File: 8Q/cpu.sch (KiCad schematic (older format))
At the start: 1 part

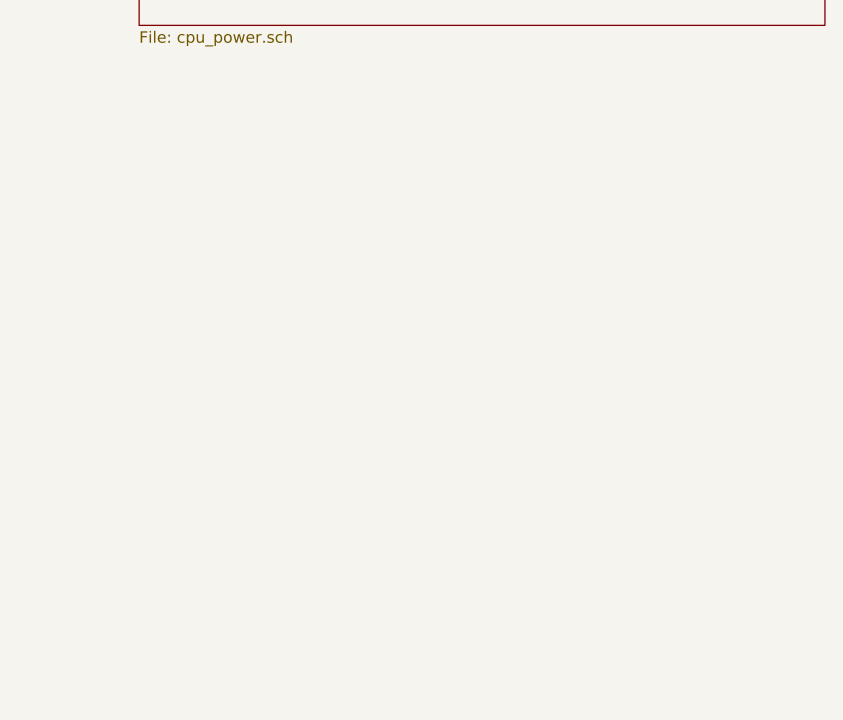
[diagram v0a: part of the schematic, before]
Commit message: modified:   8Q/8Q-cache.lib 	modified:   8Q/8Q.sch 	modified:   8Q/8_qp_io.sch 	new file:   8Q/RAM.sch 	deleted:    8Q/_saved_RAM.sch 	modified:   8Q/cpu.sch 	modified:   8Q/cpu_power.sch 	modified:   8Q/power.sch 	modified:   8Q/preprocessor.sch 	modified:   8Q/qpower.sch 	modified:   8Q/qpu.sch 	new file:   8q.dia 	modified:   README.md 	new file:   docs/source/imgs/8q.png
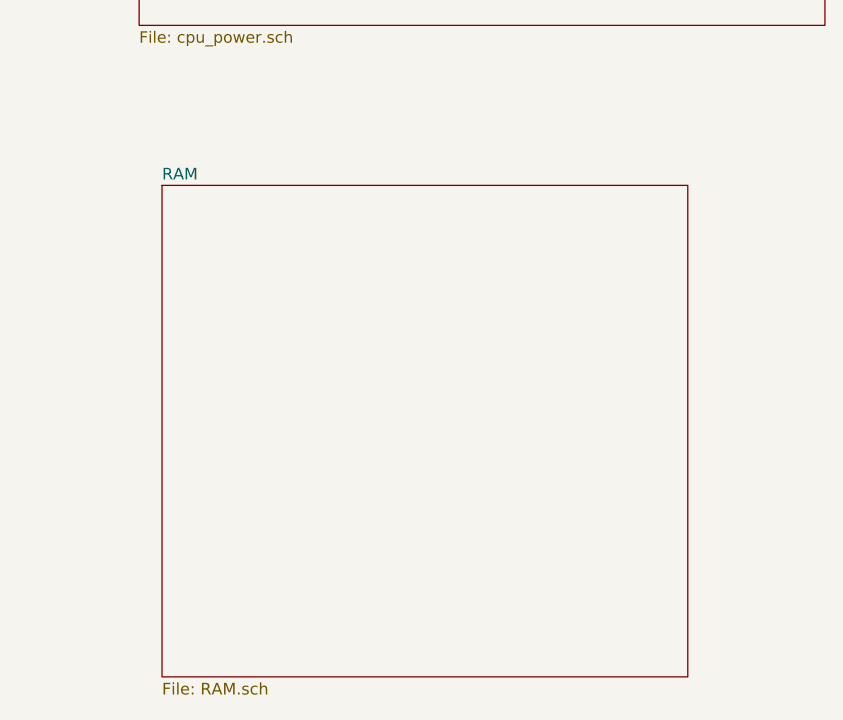
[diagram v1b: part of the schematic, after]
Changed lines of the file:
@@
 $Descr A4 11693 8268
 encoding utf-8
-Sheet 2 8
+Sheet 2 9
 Title "8Q Quantum Computer"
 Date "2020-06-29"
@@
 F1 "cpu_power.sch" 50
 $EndSheet
+$Sheet
+S 11850 3750 2300 2150
+U 5F329712
+F0 "RAM" 51
+F1 "RAM.sch" 51
+$EndSheet
 $EndSCHEMATC

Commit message: modified:   8Q/8Q-cache.lib 	modified:   8Q/8Q.sch 	modified:   8Q/8_qp_io.sch 	modified:   8Q/RAM.sch 	new file:   8Q/control_logic.sch 	modified:   8Q/cpu.sch 	modified:   8Q/cpu_power.sch 	new file:   8Q/inorder.sch 	new file:   8Q/instruction_bus.sch 	new file:   8Q/output_cache.sch 	modified:   8Q/power.sch 	modified:   8Q/preprocessor.sch 	modified:   8Q/qpower.sch 	modified:   8Q/qpu.sch 	new file:   Controller.md 	modified:   QCore.md 	new file:   QPU_Operation.md 	new file:   docs/source/imgs/Screenshot from 2020-07-07 18-04-51.png 	new file:   tools/photon_birth_death.py 	new file:   tools/processor.py
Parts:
- added J1: HDMI_A, Connector_HDMI:HDMI_A_Contact_Technology_HDMI-19APL2_Horizontal, symbol Connector:HDMI_A
- added unit 2 of U1
- added unit 3 of U1
- added unit 4 of U1
- added unit 5 of U1
- added U2: H5AN8G8NAFR-UHC, Package_BGA:FBGA-78_7.5x11mm_Layout2x3x13_P0.8mm, symbol Memory_RAM:H5AN8G8NAFR-UHC
- gave numbers to parts that had none: 1
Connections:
- net labels added: GND, HDMI_CEC, HDMI_SCL, HDMI_SDA, HDMI_UTIL, HDMI_VCC, HDMI_VDD, RAM_A0, RAM_A1, RAM_A10, RAM_A11, RAM_A12, RAM_A13, RAM_A14, RAM_A15, RAM_A16, RAM_A17, RAM_A2, RAM_A3, RAM_A4, RAM_A5, RAM_A6, RAM_A7, RAM_A8, RAM_A9, RAM_ACT, RAM_CKE0, RAM_CKE1, RAM_PARITY, RAM_RESET
- wire segments 0 -> 33
- no-connect marks 0 -> 2
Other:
- moved on the sheet: U1A

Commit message: modified:   8Q/8Q-cache.lib 	new file:   8Q/8Q-rescue.dcm 	new file:   8Q/8Q-rescue.lib 	modified:   8Q/8Q.kicad_pcb 	modified:   8Q/8Q.sch 	modified:   8Q/8_qp_io.sch 	new file:   8Q/QGates.pretty/CH-Gate.kicad_mod 	new file:   8Q/QGates.pretty/CX-Gate.kicad_mod 	new file:   8Q/QGates.pretty/CY-Gate.kicad_mod 	new file:   8Q/QGates.pretty/CZ-Gate.kicad_mod 	new file:   8Q/QGates.pretty/H-Gate.kicad_mod 	new file:   8Q/QGates.pretty/Measure.kicad_mod 	new file:   8Q/QGates.pretty/Photon-Source.kicad_mod 	new file:   8Q/QGates.pretty/X-Gate.kicad_mod 	new file:   8Q/QGates.pretty/Y-Gate.kicad_mod 	new file:   8Q/QGates.pretty/Z-Gate.kicad_mod 	modified:   8Q/control_logic.sch 	modified:   8Q/cpu.sch 	modified:   8Q/inorder.sch 	modified:   8Q/instruction_bus.sch 	modified:   8Q/output_cache.sch 	modified:   8Q/power.sch 	modified:   8Q/preprocessor.sch 	modified:   8Q/qpower.sch 	modified:   8Q/qpu.sch 	new file:   8Q/sym-lib-table Introduced embedded QSeven module to replace CPU Computer now has support for: * 10Gbps Ethernet * 1xUSB3.0 * 4xUSB2.0 * 1xJTAG * 1xCAN * 1-Wire Bus * 1xSMBus * 1xI2C * External Watchdog * HDMI * LVDS
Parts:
- removed J1: HDMI_A, Connector_HDMI:HDMI_A_Contact_Technology_HDMI-19APL2_Horizontal, symbol Connector:HDMI_A
- removed U1: ALLWINNER_H6_V200, BGA451C65P23X23_1500X1500X118N, symbol ALLWINNER_H6_V200:ALLWINNER_H6_V200
- removed U2: H5AN8G8NAFR-UHC, Package_BGA:FBGA-78_7.5x11mm_Layout2x3x13_P0.8mm, symbol Memory_RAM:H5AN8G8NAFR-UHC
- added BT1: Battery_Cell, symbol Device:Battery_Cell
- added C262292_1, C262292_2: LVDS Display, Connector_FFC-FPC:Hirose_FH12-40S-0.5SH_1x40-1MP_P0.50mm_Horizontal, symbol Connector:Conn_01x40_Female
- added D1: GreenLED, LED_SMD:LED_0603_1608Metric, symbol Device:LED
- added D10, D11, D12, D13, D14, D15, D16, D17, D18, D19, D20, D5, D6, D7, D8, D9: 1SS367,H3F, Diode_SMD:D_SOD-323, symbol Device:D_Schottky
- added D2: BlueLED, LED_SMD:LED_0603_1608Metric, symbol Device:LED
- added D3, D4: D_Small, symbol Device:D_Small
- added FL1, FL2, FL3, FL4, FL5: EMI_Filter_CommonMode, symbol Device:EMI_Filter_CommonMode
- added J1: TEMP, Connector_PinHeader_1.00mm:PinHeader_1x02_P1.00mm_Vertical, symbol Connector:Conn_01x02_Female
- added J10, J11, J16, J17: Bus_PCI_Express_x1, Connector_PCBEdge:BUS_PCIexpress_x1, symbol Connector2:Bus_PCI_Express_x1
- added J12: 8P8C_LED_Shielded, Connector_RJ:RJ45_Amphenol_54602-x08_Horizontal, symbol Connector:8P8C_LED_Shielded
- added J13: Watchdog, Connector_PinHeader_1.00mm:PinHeader_1x02_P1.00mm_Vertical, symbol Connector:Conn_01x02_Female
- added J14: Bus_PCI_Express_x4, Connector_PCBEdge:BUS_PCIexpress_x4, symbol Connector2:Bus_PCI_Express_x4
- added J15: SD_Card, Connector_Card:microSD_HC_Hirose_DM3AT-SF-PEJM5, symbol Connector2:SD_Card
- added J18: HDMI_A, symbol Connector:HDMI_A
- added J19: BIOS_DISABLE, Connector_PinHeader_1.00mm:PinHeader_1x02_P1.00mm_Vertical, symbol Connector:Conn_01x02_Female
- added J2: 1 WIRE BUS, Connector_PinHeader_1.00mm:PinHeader_1x01_P1.00mm_Vertical, symbol Connector:Conn_01x01_Female
- added J20: AVR-JTAG-10, Connector_IDC:IDC-Header_2x04_P2.54mm_Vertical, symbol Connector:AVR-JTAG-10
- added J21: USB3_A, Connector_USB:USB3_A_Molex_48393-001, symbol Connector:USB3_A
- added J22: LDC, Connector_IDC:IDC-Header_2x04_P2.54mm_Vertical, symbol Connector_Generic:Conn_02x04_Counter_Clockwise
- added J23: GPIO, Connector_PinHeader_1.00mm:PinHeader_1x08_P1.00mm_Vertical, symbol Connector:Conn_01x08_Female
- added J24, J25, J26, J27, J28: USB_A, Connector_USB:USB3_A_Molex_48393-001, symbol Connector2:USB_A
- added J3: SMBUS, Connector_PinHeader_1.00mm:PinHeader_1x03_P1.00mm_Vertical, symbol Connector:Conn_01x03_Female
- added J4: GP0_I2C, Connector_PinHeader_1.00mm:PinHeader_1x02_P1.00mm_Vertical, symbol Connector:Conn_01x02_Female
- added J5: HDA/I2C, Connector_PinHeader_1.00mm:PinHeader_1x05_P1.00mm_Vertical, symbol Connector:Conn_01x05_Female
- added J6: SATA0, Connector_SATA_SAS:SATA_Amphenol_10029364-001LF_Horizontal, symbol Connector:Conn_01x07_Female
- added J7: SATA1, Connector_SATA_SAS:SATA_Amphenol_10029364-001LF_Horizontal, symbol Connector:Conn_01x07_Female
- added J8: CAN BUS, Connector_PinHeader_1.00mm:PinHeader_1x02_P1.00mm_Vertical, symbol Connector:Conn_01x02_Female
- added J9: UART, Connector_PinHeader_1.00mm:PinHeader_1x04_P1.00mm_Vertical, symbol Connector:Conn_01x04_Male
- added M9: CPU_FAN, Connector:FanPinHeader_1x04_P2.54mm_Vertical, symbol Motor:Fan_4pin
- added Q1, Q2, Q3, Q4: Q_PNP_BCE, Package_TO_SOT_SMD:SOT-23, symbol Device:Q_PNP_BCE
- added Q5: Q_NPN_BCE, Package_TO_SOT_SMD:SOT-23, symbol Device:Q_NPN_BCE
- added Q6: Q7, Connector:MXM2.0, symbol Q7:Q7
- added R1, R2, R3, R4: 10k, Resistor_SMD:R_0402_1005Metric, symbol Device:R_Small_US
- added R10: 1M, Resistor_SMD:R_0402_1005Metric, symbol Device:R_Small_US
- added R5, R6, R7, R8: 1k, Resistor_SMD:R_0402_1005Metric, symbol Device:R_Small_US
- added R9: 10ohm, Resistor_SMD:R_0402_1005Metric, symbol Device:R_Small_US
- added U1, U180, U182, U184, U185, U186, U187, U2: USBLC6-2P6, Package_TO_SOT_SMD:SOT-666, symbol Power_Protection:USBLC6-2SC6
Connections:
- net labels added: +12V, +3.3V, +5V, BATLOW, BIOS_DISABLE, CAN0_RX, CAN0_TX, DP_HDMI_HPD, FAN_PWM, FAN_TACHO, GBE0+, GBE0-, GBE1+, GBE1-, GBE2+, GBE2-, GBE3+, GBE3-, GBE_10, GBE_100, GBE_1000, GBE_ACT, GP0_I2C_CLK, GP1_WIRE_BUS, GPO_I2C_DAT, HDA_BITCLK, HDA_RST, HDA_SDI, HDA_SDO, HDA_SYNC, HDMI_CTRL_CLK, HTMI_CTRL_DATA, JTAG_TCK, JTAG_TDI, JTAG_TDO, JTAG_TMS, JTAG_TRST, LID_BTN, LPC_AD0_GPIO0, LPC_AD1_GPIO1, LPC_AD2_GPIO2, LPC_AD3_GPIO3, LPC_CLK_GPIO4, LPC_FRAME_GPIO5, LPC_LDRQ_GPIO7, LVDS_A0+, LVDS_A0-, LVDS_A1+, LVDS_A1-, LVDS_A2+, LVDS_A2-, LVDS_A3+, LVDS_A3-, LVDS_A_CLK+, LVDS_A_CLK-, LVDS_B0+, LVDS_B0-, LVDS_B1+, LVDS_B1-, LVDS_B2+, LVDS_B2-, LVDS_B3+, LVDS_B3-, LVDS_BLC_CLK, LVDS_BLC_DAT, LVDS_BLEN, LVDS_BLT_CTRL, LVDS_B_CLK+, LVDS_B_CLK-, LVDS_DID_CLK, LVDS_DID_DAT, LVDS_PPEN, PCIE0_RX+, PCIE0_RX-, PCIE0_TX+, PCIE0_TX-, PCIE1_RX+, PCIE1_RX-, PCIE1_TX+, PCIE1_TX-, PCIE2_RX+, PCIE2_RX-, PCIE2_TX+, PCIE2_TX-, PCIE3_RX+, PCIE3_RX-, PCIE3_TX+, PCIE3_TX-, PCIE_CLK_REF+, PCIE_CLK_REF-, PCIE_RST, PCIE_WAKE, PWRBTN, RSTBTN, SATA0_RX+, SATA0_RX-, SATA0_TX+, SATA0_TX-, SATA1_RX+, SATA1_RX-, SATA1_TX+, SATA1_TX-, SATA_ACT, SDIO_CD, SDIO_CLK, SDIO_CMD, SDIO_DAT0, SDIO_DAT1, SDIO_DAT2, SDIO_DAT3, SDIO_DAT4, SDIO_DAT5, SDIO_DAT6, SDIO_DAT7, SDIO_LED, SDIO_PWR, SDIO_WP, SERIRQ_GPIO6, SLPBTN, SMCLK, SMDAT, SM_ALERT, SPI_CS0, SPI_CS1, SPI_MISO, SPI_MOSI, SPI_SCK, SPKR, SUS_STAT, ScreenLEDAnode, ScreenLEDCathode, SoftOff, SuspendToRAM, THRM, THRMTRIP, TMDS_CLK+, TMDS_CLK-, TMDS_LANE0+, TMDS_LANE0-, TMDS_LANE1+, TMDS_LANE1-, TMDS_LANE2+, TMDS_LANE2-, UART0_CTS, UART0_RTS, UART0_RX, UART0_TX, USB_ID, USB_P0+, USB_P0-, USB_P1+, USB_P1-, USB_P2+, USB_P2-, USB_P3+, USB_P3-, USB_P4+, USB_P4-, USB_P5+, USB_P5-, USB_RX0+, USB_RX0-, USB_TX0+, USB_TX0-, USB_VBUS, WAKE, WDOUT, WDTRIG
- net labels removed: HDMI_CEC, HDMI_SCL, HDMI_SDA, HDMI_UTIL, HDMI_VCC, HDMI_VDD, RAM_A0, RAM_A1, RAM_A10, RAM_A11, RAM_A12, RAM_A13, RAM_A14, RAM_A15, RAM_A16, RAM_A17, RAM_A2, RAM_A3, RAM_A4, RAM_A5, RAM_A6, RAM_A7, RAM_A8, RAM_A9, RAM_ACT, RAM_CKE0, RAM_CKE1, RAM_PARITY, RAM_RESET
- wire segments 33 -> 334
- no-connect marks 2 -> 93
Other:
- note added: "PCIe Ports"
